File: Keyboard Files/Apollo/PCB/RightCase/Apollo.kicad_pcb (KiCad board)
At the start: 2 copper layers, 151.9 x 125.5 mm, 90 parts, among them J2 AVR-ISP-6, SW2 SW_Push, U3 PRTR5V0U2X, U4 ATmega32U4-MU, Y2 Crystal_GND24_Small

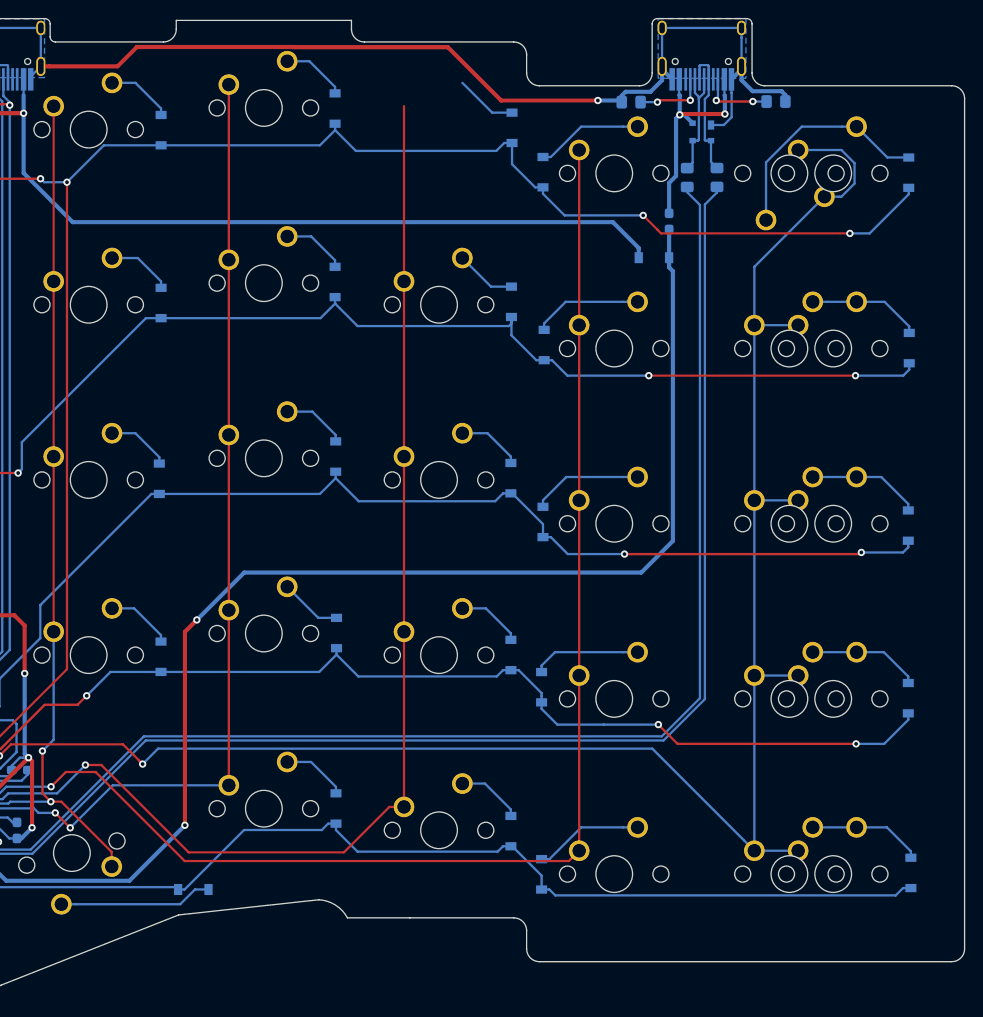
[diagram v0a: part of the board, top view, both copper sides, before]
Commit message: Update Apollo plates, export pcb and plate svgs
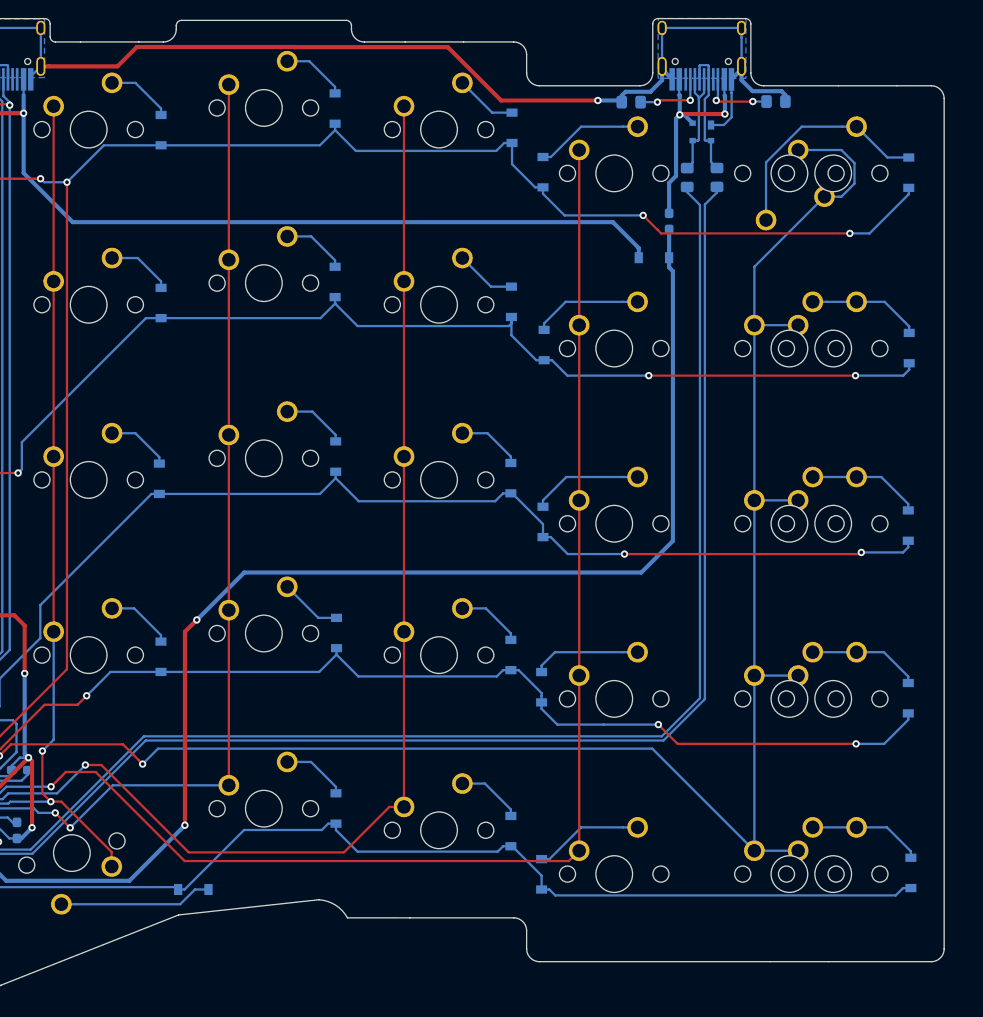
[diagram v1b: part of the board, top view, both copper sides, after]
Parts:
- added MX35: MX-NoLED, MX_Only:MXOnly-1U-NoLED, F.Cu at (311.7, 70.9)
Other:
- board size 151.9 x 125.5 mm -> 149.7 x 125.5 mm

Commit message: Increase Apollo plate bezel
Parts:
- added C1: 0.1uF, Capacitor_SMD:C_0603_1608Metric_Pad1.05x0.95mm_HandSolder, B.Cu at (163.3, 146.7)
- added C2: 0.1uF, Capacitor_SMD:C_0603_1608Metric_Pad1.05x0.95mm_HandSolder, B.Cu at (171.9, 151.1)
- added C3: 0.1uF, Capacitor_SMD:C_0603_1608Metric_Pad1.05x0.95mm_HandSolder, B.Cu at (175.1, 136.8)
- added C4: 10uF, Capacitor_SMD:C_0603_1608Metric_Pad1.05x0.95mm_HandSolder, B.Cu at (163.2, 140.0)
- added C5: 22pF, Capacitor_SMD:C_0603_1608Metric_Pad1.05x0.95mm_HandSolder, B.Cu at (181.5, 147.0)
- added C6: 22pF, Capacitor_SMD:C_0603_1608Metric_Pad1.05x0.95mm_HandSolder, B.Cu at (180.9, 141.7)
- added C7: 1uF, Capacitor_SMD:C_0603_1608Metric_Pad1.05x0.95mm_HandSolder, B.Cu at (170.0, 136.6)
- added D1: D_Small, Diode_SMD:D_SOD-123, B.Cu at (66.2, 75.8)
- added D10: D_Small, Diode_SMD:D_SOD-123, B.Cu at (143.4, 87.5)
- added D11: D_Small, Diode_SMD:D_SOD-123, B.Cu at (146.8, 89.8)
- added D12: D_Small, Diode_SMD:D_SOD-123, B.Cu at (181.1, 92.1)
- added D13: Schottky, Diode_SMD:D_SOD-123, B.Cu at (83.9, 85.9)
- added D14: D_Small, Diode_SMD:D_SOD-123, B.Cu at (80.9, 119.5)
- added D15: D_Small, Diode_SMD:D_SOD-123, B.Cu at (105.1, 113.6)
- added D16: D_Small, Diode_SMD:D_SOD-123, B.Cu at (124.1, 109.0)
- added D17: D_Small, Diode_SMD:D_SOD-123, B.Cu at (143.3, 106.5)
- added D18: D_Small, Diode_SMD:D_SOD-123, B.Cu at (146.9, 108.8)
- added D19: D_Small, Diode_SMD:D_SOD-123, B.Cu at (181.2, 111.4)
- added D2: D_Small, Diode_SMD:D_SOD-123, B.Cu at (105.2, 75.7)
- added D20: D_Small, Diode_SMD:D_SOD-123, B.Cu at (66.1, 132.7)
- added D21: D_Small, Diode_SMD:D_SOD-123, B.Cu at (105.2, 132.7)
- added D22: D_Small, Diode_SMD:D_SOD-123, B.Cu at (124.1, 128.1)
- added D23: D_Small, Diode_SMD:D_SOD-123, B.Cu at (143.2, 125.7)
- added D24: D_Small, Diode_SMD:D_SOD-123, B.Cu at (146.9, 128.1)
- added D25: D_Small, Diode_SMD:D_SOD-123, B.Cu at (181.4, 130.5)
- added D26: D_Small, Diode_SMD:D_SOD-123, B.Cu at (66.4, 151.6)
- added D27: D_Small, Diode_SMD:D_SOD-123, B.Cu at (105.2, 151.8)
- added D28: D_Small, Diode_SMD:D_SOD-123, B.Cu at (124.3, 147.0)
- added D29: D_Small, Diode_SMD:D_SOD-123, B.Cu at (143.3, 144.9)
- added D3: D_Small, Diode_SMD:D_SOD-123, B.Cu at (124.3, 71.0)
- added D30: D_Small, Diode_SMD:D_SOD-123, B.Cu at (158.6, 157.7)
- added D31: D_Small, Diode_SMD:D_SOD-123, B.Cu at (173.3, 159.7)
- added D32: D_Small, Diode_SMD:D_SOD-123, B.Cu at (189.6, 169.7)
- added D4: D_Small, Diode_SMD:D_SOD-123, B.Cu at (143.2, 68.6)
- added D5: D_Small, Diode_SMD:D_SOD-123, B.Cu at (147.0, 70.9)
- added D6: D_Small, Diode_SMD:D_SOD-123, B.Cu at (181.2, 73.3)
- added D7: D_Small, Diode_SMD:D_SOD-123, B.Cu at (66.2, 94.6)
- added D8: D_Small, Diode_SMD:D_SOD-123, B.Cu at (105.1, 94.6)
- added D9: D_Small, Diode_SMD:D_SOD-123, B.Cu at (124.5, 89.7)
- added F1: 500mA, Fuse:Fuse_0603_1608Metric_Pad1.05x0.95mm_HandSolder, B.Cu at (84.0, 81.3)
- added J1: AVR-ISP-6, Molex-0548190589:Reset_Pretty-Mask, F.Cu at (190.1, 159.1)
- added J10: Conn_01x01, locallib:breakaway-mousebites, F.Cu at (122.9, 161.4)
- added J11: Conn_01x01, locallib:breakaway-mousebites, F.Cu at (358.3, 66.2)
- added J12: Conn_01x01, locallib:breakaway-mousebites, F.Cu at (350.8, 161.4)
- added J13: Conn_01x01, locallib:breakaway-mousebites, F.Cu at (305.3, 161.4)
- added J14: Conn_01x01, locallib:breakaway-mousebites, F.Cu at (305.3, 156.7)
- added J15: Conn_01x01, locallib:breakaway-mousebites, F.Cu at (69.2, 61.4)
- added J16: Conn_01x01, locallib:breakaway-mousebites, F.Cu at (358.3, 61.4)
- added J17: Conn_01x01, Connector_PinHeader_2.54mm:PinHeader_1x01_P2.54mm_Vertical, F.Cu at (180.9, 123.5)
- added J3: Conn_01x01, locallib:breakaway-mousebites, F.Cu at (69.2, 66.2)
- added J4: Conn_01x01, locallib:breakaway-mousebites, F.Cu at (116.6, 61.4)
- added J5: Conn_01x01, locallib:breakaway-mousebites, F.Cu at (311.1, 61.4)
- added J6: Conn_01x01, locallib:breakaway-mousebites, F.Cu at (153.0, 61.4)
- added J7: Conn_01x01, locallib:breakaway-mousebites, F.Cu at (275.8, 61.4)
- added J8: Conn_01x01, locallib:breakaway-mousebites, F.Cu at (77.5, 161.4)
- added J9: Conn_01x01, locallib:breakaway-mousebites, F.Cu at (122.9, 156.7)
- added JP1: Jumper_NO, Jumper:SolderJumper-2_P1.3mm_Open_Pad1.0x1.5mm, B.Cu at (171.3, 155.4)
- added MX1: MX-NoLED, MX_Only:MXOnly-1.5U-NoLED, F.Cu at (73.7, 75.7)
- added MX10: MX-NoLED, MX_Only:MXOnly-1U-NoLED, F.Cu at (135.6, 87.6)
- added MX11: MX-NoLED, MX_Only:MXOnly-1U-NoLED, F.Cu at (154.6, 90.0)
- added MX12: MX-NoLED, MX_Only:MXOnly-1U-NoLED, F.Cu at (173.7, 92.4)
- added MX13: MX-NoLED, MX_Only:MXOnly-1.5U-NoLED, F.Cu at (73.7, 113.8)
- added MX14: MX-NoLED, MX_Only:MXOnly-1U-NoLED, F.Cu at (97.5, 113.8)
- added MX15: MX-NoLED, MX_Only:MXOnly-1U-NoLED, F.Cu at (116.5, 109.0)
- added MX16: MX-NoLED, MX_Only:MXOnly-1U-NoLED, F.Cu at (135.6, 106.7)
- added MX17: MX-NoLED, MX_Only:MXOnly-1U-NoLED, F.Cu at (154.6, 109.0)
- added MX18: MX-NoLED, MX_Only:MXOnly-1U-NoLED, F.Cu at (173.7, 111.4)
- added MX19: MX-NoLED, MX_Only:MXOnly-1.5U-NoLED, F.Cu at (73.7, 132.8)
- added MX2: MX-NoLED, MX_Only:MXOnly-1U-NoLED, F.Cu at (97.5, 75.7)
- added MX20: MX-NoLED, MX_Only:MXOnly-1U-NoLED, F.Cu at (97.5, 132.8)
- added MX21: MX-NoLED, MX_Only:MXOnly-1U-NoLED, F.Cu at (116.5, 128.1)
- added MX22: MX-NoLED, MX_Only:MXOnly-1U-NoLED, F.Cu at (135.6, 125.7)
- added MX23: MX-NoLED, MX_Only:MXOnly-1U-NoLED, F.Cu at (154.6, 128.1)
- added MX24: MX-NoLED, MX_Only:MXOnly-1U-NoLED, F.Cu at (173.7, 130.5)
- added MX25: MX-NoLED, MX_Only:MXOnly-1.5U-NoLED, F.Cu at (73.7, 151.9)
- added MX26: MX-NoLED, MX_Only:MXOnly-1U-NoLED, F.Cu at (97.5, 151.9)
- added MX27: MX-NoLED, MX_Only:MXOnly-1U-NoLED, F.Cu at (116.5, 147.1)
- added MX28: MX-NoLED, MX_Only:MXOnly-1U-NoLED, F.Cu at (135.6, 144.8)
- added MX29: MX-NoLED, MX_Only:MXOnly-1U-NoLED, F.Cu at (156.5, 149.6)
- added MX3: MX-NoLED, MX_Only:MXOnly-1U-NoLED, F.Cu at (116.5, 70.9)
- added MX30: MX-NoLED, MX_Only:MXOnly-1.5U-Vertical-NoLED, F.Cu at (179.9, 157.2)
- added MX31: MX-NoLED, MX_Only:MXOnly-1.5U-Vertical-NoLED, F.Cu at (195.8, 167.5)
- added MX4: MX-NoLED, MX_Only:MXOnly-1U-NoLED, F.Cu at (135.6, 68.6)
- added MX5: MX-NoLED, MX_Only:MXOnly-1U-NoLED, F.Cu at (154.6, 70.9)
- added MX6: MX-NoLED, MX_Only:MXOnly-1U-NoLED, F.Cu at (173.7, 73.3)
- added MX63: MX-NoLED, MX_Only:MXOnly-1U-NoLED, F.Cu at (78.4, 75.7)
- added MX64: MX-NoLED, MX_Only:MXOnly-1U-NoLED, F.Cu at (78.4, 94.7)
- added MX65: MX-LED, MX_Only:MXOnly-1U, F.Cu at (78.4, 113.8)
- added MX66: MX-NoLED, MX_Only:MXOnly-1U-NoLED, F.Cu at (78.4, 132.8)
- added MX67: MX-NoLED, MX_Only:MXOnly-1U-NoLED, F.Cu at (78.4, 151.9)
- added MX7: MX-NoLED, MX_Only:MXOnly-1.5U-NoLED, F.Cu at (73.7, 94.7)
- added MX8: MX-NoLED, MX_Only:MXOnly-1U-NoLED, F.Cu at (97.5, 94.7)
- added MX9: MX-NoLED, MX_Only:MXOnly-1U-NoLED, F.Cu at (116.5, 90.0)
- added R1: 10k, Resistor_SMD:R_0805_2012Metric_Pad1.15x1.40mm_HandSolder, B.Cu at (167.7, 156.2)
- added R2: 10k, Resistor_SMD:R_0805_2012Metric_Pad1.15x1.40mm_HandSolder, B.Cu at (169.2, 119.0)
- added R3: 22, Resistor_SMD:R_0805_2012Metric_Pad1.15x1.40mm_HandSolder, B.Cu at (89.6, 76.8)
- added R4: 22, Resistor_SMD:R_0805_2012Metric_Pad1.15x1.40mm_HandSolder, B.Cu at (86.3, 76.9)
- added R5: 5.1k, Resistor_SMD:R_0805_2012Metric_Pad1.15x1.40mm_HandSolder, B.Cu at (94.7, 68.1)
- added R6: 5.1k, Resistor_SMD:R_0805_2012Metric_Pad1.15x1.40mm_HandSolder, B.Cu at (80.8, 68.2)
- added R7: 10k, Resistor_SMD:R_0805_2012Metric_Pad1.15x1.40mm_HandSolder, B.Cu at (164.5, 149.4)
- added R8: 4.7k, Resistor_SMD:R_0805_2012Metric_Pad1.15x1.40mm_HandSolder, B.Cu at (165.9, 73.4)
- added R9: 4.7k, Resistor_SMD:R_0805_2012Metric_Pad1.15x1.40mm_HandSolder, B.Cu at (162.4, 73.4)
- added SW1: SW_Push, locallib:SKQGADE010, B.Cu at (176.3, 118.9)
- added U1: PRTR5V0U2X, locallib:SOT143B, B.Cu at (87.9, 71.4)
- added U2: ATmega32U4-MU, Package_DFN_QFN:QFN-44-1EP_7x7mm_P0.5mm_EP5.2x5.2mm, B.Cu at (169.7, 144.1)
- added USB1: HRO-TYPE-C-31-M-12, Type-C:HRO-TYPE-C-31-M-12-HandSoldering, B.Cu at (87.9, 57.3)
- added USB2: HRO-TYPE-C-31-M-12, Type-C:HRO-TYPE-C-31-M-12-HandSoldering, B.Cu at (164.1, 57.3)
- added Y1: Crystal_GND24_Small, Crystal:Crystal_SMD_3225-4Pin_3.2x2.5mm_HandSoldering, B.Cu at (178.5, 144.1)
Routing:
- net GND: track 0.00 -> 364.1 mm, vias 0 -> 2
- net +5V: track 0.00 -> 283.2 mm, vias 0 -> 16
- net Row0: track 0.00 -> 222.3 mm, vias 0 -> 6
- net Col0: track 0.00 -> 207.8 mm, vias 0 -> 2
- net Row1: track 0.00 -> 196.7 mm, vias 0 -> 6
- net Col1: track 0.00 -> 161.3 mm, vias 0 -> 3
- net Row2: track 0.00 -> 158.7 mm, vias 0 -> 6
- net Row3: track 0.00 -> 156.6 mm, vias 0 -> 4
- net Row4: track 0.00 -> 153.8 mm, vias 0 -> 2
- net VBUS: track 0.00 -> 150.9 mm, vias 0 -> 6
- net Col2: track 0.00 -> 144.1 mm, vias 0 -> 3
- net D-: track 0.00 -> 140.5 mm
- net D+: track 0.00 -> 139.7 mm
- net Col5: track 0.00 -> 137.3 mm, vias 0 -> 3
- net CapsLED: track 0.00 -> 128.3 mm, vias 0 -> 3
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- added copper zone on B.Cu, net GND
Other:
- board size 149.7 x 125.5 mm -> 309.8 x 159.1 mm
